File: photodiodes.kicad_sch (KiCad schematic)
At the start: 54 parts, among them U19 OPA380AIDGKT, U20 OPA380AIDGKT, U21 OPA380AIDGKT, U22 OPA380AIDGKT, U23 OPA380AIDGKT, U24 OPA380AIDGKT, U25 OPA380AIDGKT, U26 OPA380AIDGKT, U27 OPA380AIDGKT, U28 OPA380AIDGKT, U29 OPA380AIDGKT, U30 OPA380AIDGKT, U31 OPA380AIDGKT, U32 OPA380AIDGKT, U33 OPA380AIDGKT, U34 OPA380AIDGKT, U35 OPA380AIDGKT, U36 OPA380AIDGKT

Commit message: Add h-bridges for magnetorquers
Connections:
- net +3.3VP renamed +3V3

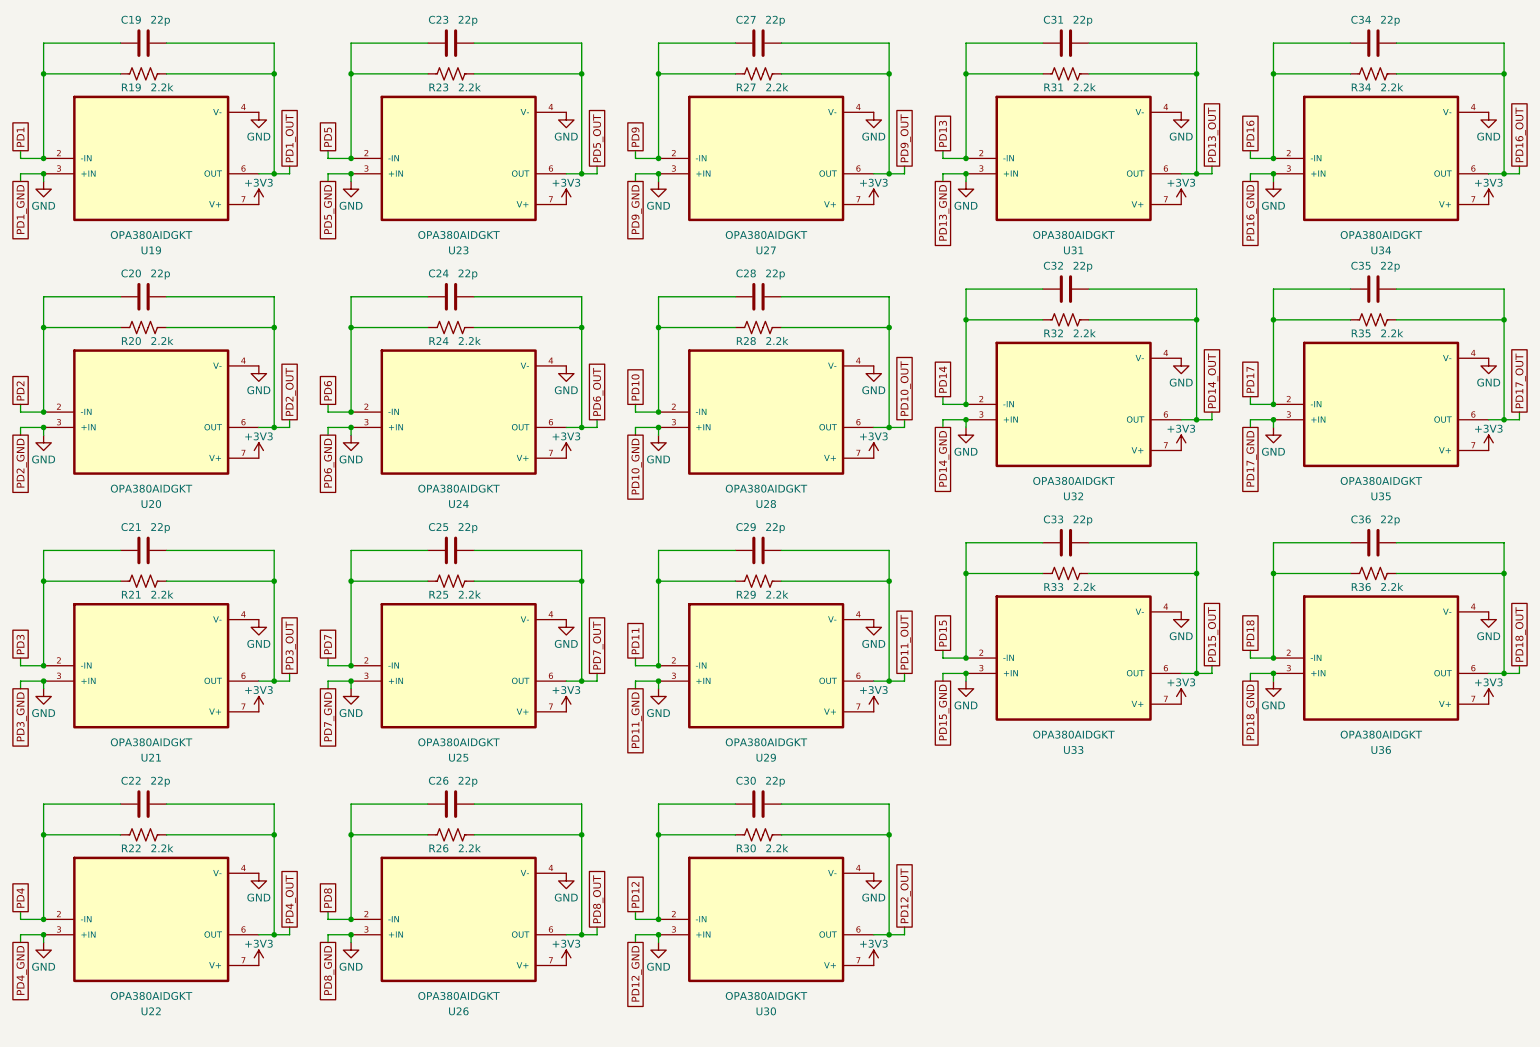
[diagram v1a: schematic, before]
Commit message: Change photodiodes to use OPA2381
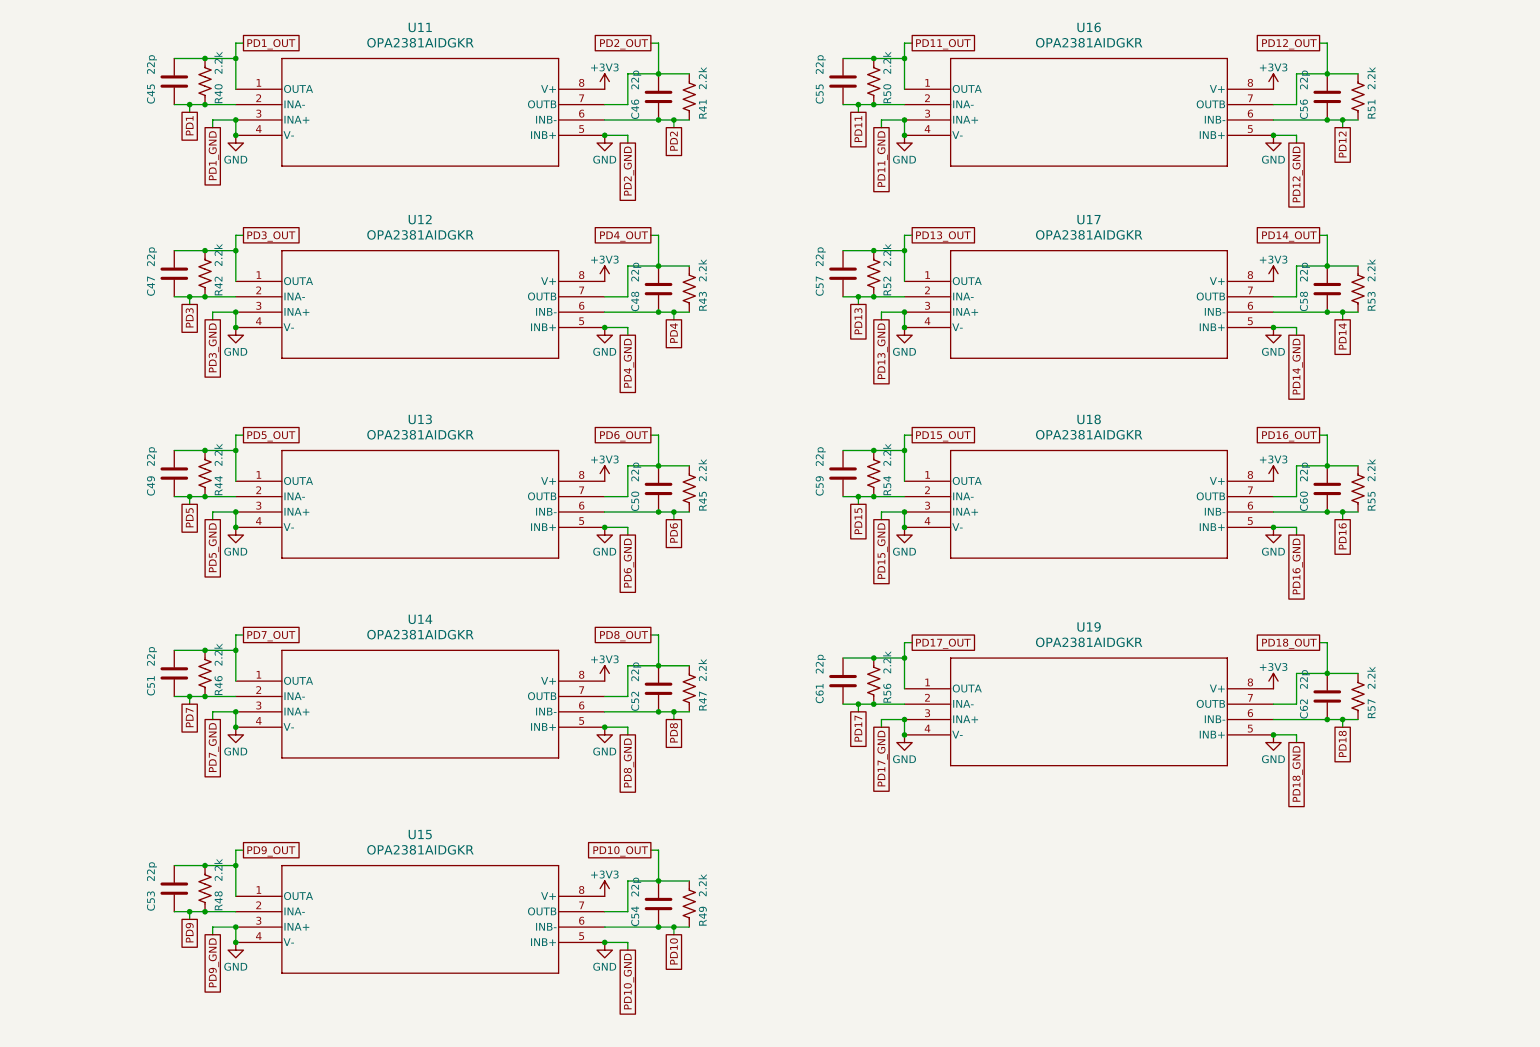
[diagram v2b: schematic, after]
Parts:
- removed C19, C20, C21, C22, C23, C24, C25, C26, C27, C28, C29, C30, C31, C32, C33, C34, C35, C36: 22p, symbol Device:C
- removed R19, R20, R21, R22, R23, R24, R25, R26, R27, R28, R29, R30, R31, R32, R33, R34, R35, R36: 2.2k, symbol Device:R_US
- removed U19, U20, U21, U22, U23, U24, U25, U26, U27, U28, U29, U30, U31, U32, U33, U34, U35, U36: OPA380AIDGKT, OPA380AIDGKT:SOP65P490X110-8N, symbol OPA380:OPA380AIDGKT
- added C45, C46, C47, C48, C49, C50, C51, C52, C53, C54, C55, C56, C57, C58, C59, C60, C61, C62: 22p, symbol Device:C
- added R40, R41, R42, R43, R44, R45, R46, R47, R48, R49, R50, R51, R52, R53, R54, R55, R56, R57: 2.2k, symbol Device:R_US
- added U11, U12, U13, U14, U15, U16, U17, U18, U19: OPA2381AIDGKR, DGK8, symbol OPA2381AIDGKR:OPA2381AIDGKR
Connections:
- net +3V3: now also U11.8 (V+), U12.8 (V+), U13.8 (V+), U14.8 (V+), U15.8 (V+), U16.8 (V+), U17.8 (V+), U18.8 (V+), U19.8 (V+)
- net GND: now also U11.3 (INA+), U11.4 (V-), U11.5 (INB+), U12.3 (INA+), U12.4 (V-), U12.5 (INB+), U13.3 (INA+), U13.4 (V-), U13.5 (INB+), U14.3 (INA+), U14.4 (V-), U14.5 (INB+), U15.3 (INA+), U15.4 (V-), U15.5 (INB+), U16.3 (INA+), U16.4 (V-), U16.5 (INB+), U17.3 (INA+), U17.4 (V-), U17.5 (INB+), U18.3 (INA+), U18.4 (V-), U18.5 (INB+), U19.3 (INA+), U19.4 (V-), U19.5 (INB+)
- net PD1: now also C45.1, R40.1, U11.2 (INA-)
- net PD10: now also C54.1, R49.1, U15.6 (INB-)
- net PD10_OUT: now also C54.2, R49.2, U15.7 (OUTB)
- net PD11: now also C55.1, R50.1, U16.2 (INA-)
- net PD11_OUT: now also C55.2, R50.2, U16.1 (OUTA)
- net PD12: now also C56.1, R51.1, U16.6 (INB-)
- net PD12_OUT: now also C56.2, R51.2, U16.7 (OUTB)
- net PD13: now also C57.1, R52.1, U17.2 (INA-)
- net PD13_OUT: now also C57.2, R52.2, U17.1 (OUTA)
- net PD14: now also C58.1, R53.1, U17.6 (INB-)
- net PD14_OUT: now also C58.2, R53.2, U17.7 (OUTB)
- net PD15: now also C59.1, R54.1, U18.2 (INA-)
- net PD15_OUT: now also C59.2, R54.2, U18.1 (OUTA)
- net PD16: now also C60.1, R55.1, U18.6 (INB-)
- net PD16_OUT: now also C60.2, R55.2, U18.7 (OUTB)
- net PD17: now also C61.1, R56.1, U19.2 (INA-)
- net PD17_OUT: now also C61.2, R56.2, U19.1 (OUTA)
- net PD18: now also C62.1, R57.1, U19.6 (INB-)
- net PD18_OUT: now also C62.2, R57.2, U19.7 (OUTB)
- net PD1_OUT: now also C45.2, R40.2, U11.1 (OUTA)
- net PD2: now also C46.1, R41.1, U11.6 (INB-)
- net PD2_OUT: now also C46.2, R41.2, U11.7 (OUTB)
- net PD3: now also C47.1, R42.1, U12.2 (INA-)
- net PD3_OUT: now also C47.2, R42.2, U12.1 (OUTA)
- net PD4: now also C48.1, R43.1, U12.6 (INB-)
- net PD4_OUT: now also C48.2, R43.2, U12.7 (OUTB)
- net PD5: now also C49.1, R44.1, U13.2 (INA-)
- net PD5_OUT: now also C49.2, R44.2, U13.1 (OUTA)
- net PD6: now also C50.1, R45.1, U13.6 (INB-)
- net PD6_OUT: now also C50.2, R45.2, U13.7 (OUTB)
- net PD7: now also C51.1, R46.1, U14.2 (INA-)
- net PD7_OUT: now also C51.2, R46.2, U14.1 (OUTA)
- net PD8: now also C52.1, R47.1, U14.6 (INB-)
- net PD8_OUT: now also C52.2, R47.2, U14.7 (OUTB)
- net PD9: now also C53.1, R48.1, U15.2 (INA-)
- net PD9_OUT: now also C53.2, R48.2, U15.1 (OUTA)
